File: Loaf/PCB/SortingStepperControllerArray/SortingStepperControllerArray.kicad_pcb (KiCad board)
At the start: 2 copper layers, 100 x 73 mm, 26 parts, among them J1 Conn_01x04_Socket, J2 Conn_01x04_Socket, J3 Conn_01x04_Socket, J4 Conn_01x04_Socket, J5 Motor_Supply, J6 Logic_Supply, J7 Logic_Input, SW1 Limit_Switch, SW2 Limit_Switch, SW3 Limit_Switch, SW4 Limit_Switch

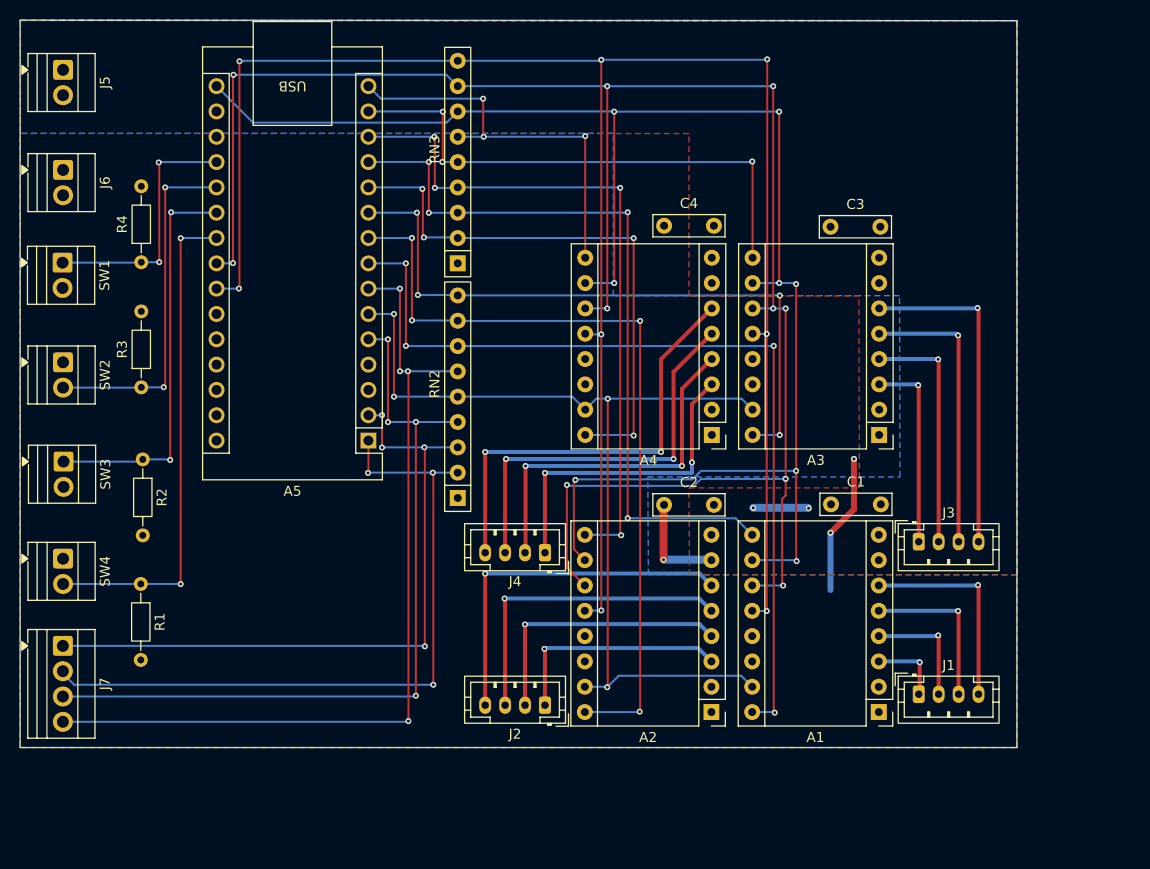
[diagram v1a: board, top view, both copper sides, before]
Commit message: Reoriented board for less signal interference
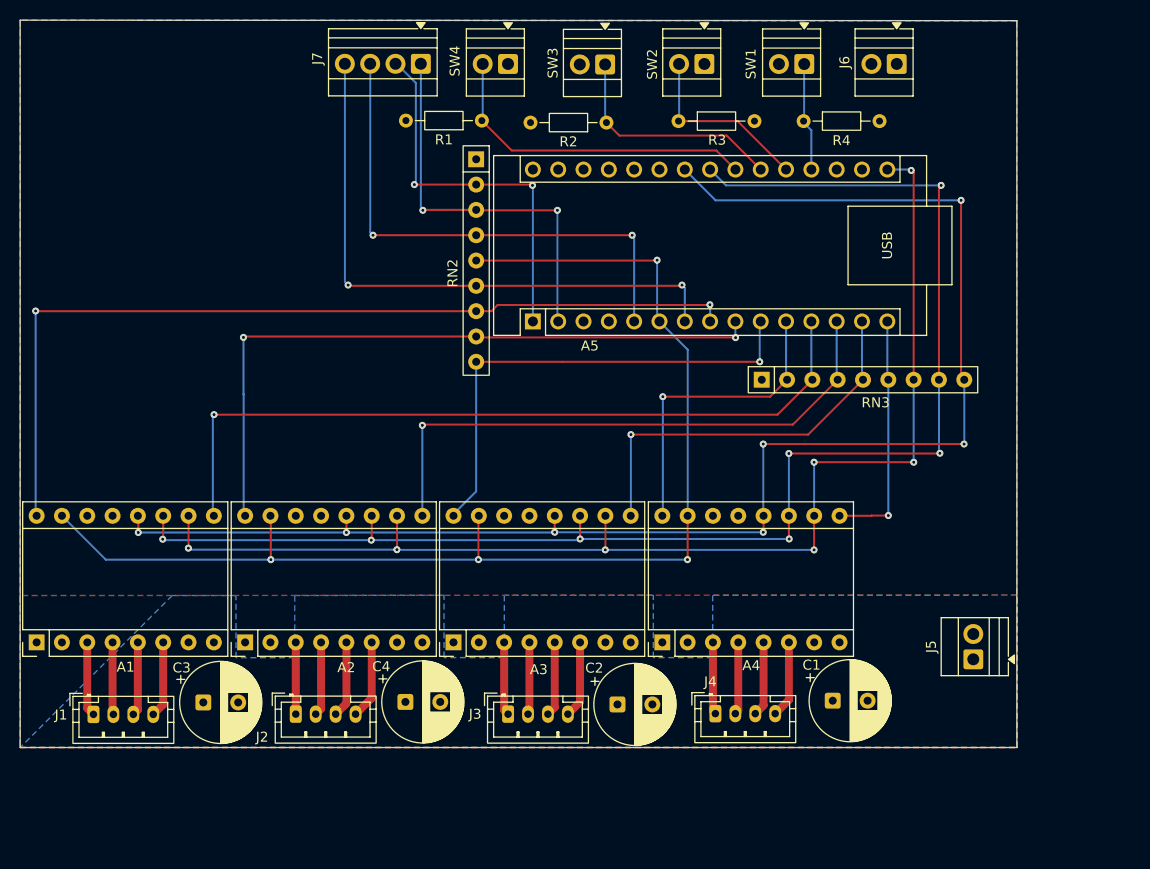
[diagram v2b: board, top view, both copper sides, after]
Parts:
- C1, C2, C3, C4: footprint Capacitor_THT:C_Rect_L7.0mm_W2.0mm_P5.00mm -> Capacitor_THT:CP_Radial_D8.0mm_P3.50mm
- moved J5 108.8 mm to (193.2, 120.5), turned to 90 degrees
- moved A1 84.8 mm to (99.2, 118.8), turned to 90 degrees
- moved J6 84.3 mm to (185.5, 60.8), turned to 180 degrees
- moved J1 82.8 mm to (105.0, 126.1)
- moved C3 79.0 mm to (116.0, 124.9)
- moved SW1 77.0 mm to (176.3, 60.8), turned to 180 degrees
- moved SW2 71.0 mm to (166.2, 60.8), turned to 180 degrees
- moved J7 68.6 mm to (137.8, 60.8), turned to 180 degrees
- moved R4 67.9 mm to (176.2, 66.5), turned to 0 degrees
- moved SW3 67.4 mm to (156.3, 60.9), turned to 180 degrees
- moved SW4 66.8 mm to (146.5, 60.8), turned to 180 degrees
- moved R3 60.2 mm to (163.7, 66.5), turned to 0 degrees
- moved R1 57.7 mm to (143.9, 66.5), turned to 180 degrees
- moved R2 57.5 mm to (156.4, 66.7), turned to 180 degrees
- moved C4 54.4 mm to (136.2, 124.8)
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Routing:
- net /MODE_1: track 189.6 -> 144.7 mm, vias 10 -> 7
- net /MODE_2: track 194.9 -> 150.4 mm, vias 8 -> 7
- net /MODE_0: track 163.9 -> 123.6 mm, vias 8 -> 7
- net Net-(A4-B2): track 44.3 -> 7.72 mm, vias 2 -> 0
- net Net-(A4-B1): track 40.4 -> 7.50 mm, vias 2 -> 0
- net /Motor_2: track 71.5 -> 38.7 mm, vias 3 -> 2
- net /Motor_1: track 68.8 -> 39.6 mm, vias 4 -> 2
- net Net-(A4-A1): track 36.4 -> 7.27 mm, vias 2 -> 0
- net Net-(A2-B2): track 36.4 -> 7.87 mm, vias 1 -> 0
- net /Motor_3: track 80.4 -> 52.2 mm, vias 4 -> 2
- net /STEP: track 95.0 -> 122.9 mm
- net /Motor_4: track 87.3 -> 59.8 mm, vias 4 -> 2
- net Net-(A3-B2): track 33.4 -> 7.71 mm, vias 1 -> 0
- net Net-(A4-A2): track 32.4 -> 7.25 mm, vias 2 -> 0
- net /Motor_4_DIR: track 56.2 -> 31.0 mm, vias 4 -> 1
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
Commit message: Redid the stepper board
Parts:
- removed A5: Arduino_Nano_Every, Module:Arduino_Nano
- removed RN2, RN3: 10K Resistor Array, Resistor_THT:R_Array_SIP9
- added A6: RaspberryPi_Pico, Module:RaspberryPi_Pico_Common_Unspecified, F.Cu at (180.3, 94.1)
- added H1: MountingHole_Pad, MountingHole:MountingHole_3.2mm_M3_DIN965_Pad, F.Cu at (113.0, 68.5)
- added H2: MountingHole_Pad, MountingHole:MountingHole_3.2mm_M3_DIN965_Pad, F.Cu at (205.0, 68.5)
- added H3: MountingHole_Pad, MountingHole:MountingHole_3.2mm_M3_DIN965_Pad, F.Cu at (113.0, 109.5)
- added H4: MountingHole_Pad, MountingHole:MountingHole_3.2mm_M3_DIN965_Pad, F.Cu at (205.0, 109.5)
- added Logo1: Logo_Open_Hardware_Small, Symbol:OSHW-Symbol_6.7x6mm_SilkScreen, F.Cu at (120.3, 68.6)
- added R5: 10K, Resistor_SMD:R_1206_3216Metric_Pad1.30x1.75mm_HandSolder, B.Cu at (176.5, 120.9)
- added R6: 10K, Resistor_SMD:R_1206_3216Metric_Pad1.30x1.75mm_HandSolder, B.Cu at (158.8, 120.9)
- added R7: 10K, Resistor_SMD:R_1206_3216Metric_Pad1.30x1.75mm_HandSolder, B.Cu at (197.8, 111.5)
- added R8: 10K, Resistor_SMD:R_1206_3216Metric_Pad1.30x1.75mm_HandSolder, B.Cu at (181.6, 120.9)
- added RN1: 10K Resistor Array, Resistor_THT:R_Array_SIP9, F.Cu at (201.9, 80.9)
- J1, J2, J3, J4: footprint Connector_JST:JST_PH_B4B-PH-K_1x04_P2.00mm_Vertical -> Connector_JST:JST_XH_B4B-XH-A_1x04_P2.50mm_Vertical
- R1, R2, R3, R4: footprint Resistor_THT:R_Axial_DIN0204_L3.6mm_D1.6mm_P7.62mm_Horizontal -> Resistor_SMD:R_1206_3216Metric_Pad1.30x1.75mm_HandSolder; moved to B.Cu
- moved R2 68.7 mm to (113.0, 119.9), turned to 90 degrees
- moved R4 67.7 mm to (135.9, 120.9), turned to 90 degrees
- moved C4 66.6 mm to (201.9, 136.0), turned to 90 degrees
- moved C3 64.1 mm to (179.1, 136.0), turned to 90 degrees
- moved R1 56.0 mm to (130.8, 120.9), turned to 90 degrees
- moved R3 55.2 mm to (153.7, 120.8), turned to 90 degrees
- moved C1 47.1 mm to (133.3, 136.0), turned to 90 degrees
- moved J4 28.2 mm to (194.3, 134.4), turned to 180 degrees
- moved J3 26.2 mm to (171.4, 134.4), turned to 180 degrees
- moved J2 24.7 mm to (148.6, 134.4), turned to 180 degrees
- moved J7 24.3 mm to (160.8, 68.7)
- moved SW4 24.0 mm to (169.2, 68.7)
- moved J1 22.3 mm to (125.7, 134.4), turned to 180 degrees
- moved A4 21.6 mm to (181.6, 128.0)
- moved SW3 21.2 mm to (176.0, 68.7)
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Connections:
- A1 pad 1: GND2 -> GND
- A1 pad 15: /STEP -> /Step1
- A1 pad 2: GND2 -> GND
- A1 pad 7: GND1 -> GND
- A2 pad 1: GND2 -> GND
- A2 pad 15: /STEP -> /Step2
- A2 pad 2: GND2 -> GND
- A2 pad 7: GND1 -> GND
- A3 pad 1: GND2 -> GND
- A3 pad 15: /STEP -> /Step3
- A3 pad 2: GND2 -> GND
- A3 pad 7: GND1 -> GND
- A4 pad 1: GND2 -> GND
- A4 pad 15: /STEP -> /Step4
- A4 pad 2: GND2 -> GND
- A4 pad 7: GND1 -> GND
- C1 pad 1: GND1 -> GND
- C2 pad 1: GND1 -> GND
- C3 pad 1: GND1 -> GND
- C4 pad 1: GND1 -> GND
- J1 pad 1: Net-(A1-A2) -> Net-(A1-B2)
- J1 pad 2: Net-(A1-A1) -> Net-(A1-B1)
- J1 pad 3: Net-(A1-B1) -> Net-(A1-A1)
- J1 pad 4: Net-(A1-B2) -> Net-(A1-A2)
- J2 pad 1: Net-(A2-A2) -> Net-(A2-B2)
- J2 pad 2: Net-(A2-A1) -> Net-(A2-B1)
- J2 pad 3: Net-(A2-B1) -> Net-(A2-A1)
- J2 pad 4: Net-(A2-B2) -> Net-(A2-A2)
- J3 pad 1: Net-(A3-A2) -> Net-(A3-B2)
- J3 pad 2: Net-(A3-A1) -> Net-(A3-B1)
- J3 pad 3: Net-(A3-B1) -> Net-(A3-A1)
- J3 pad 4: Net-(A3-B2) -> Net-(A3-A2)
- J4 pad 1: Net-(A4-A2) -> Net-(A4-B2)
- J4 pad 2: Net-(A4-A1) -> Net-(A4-B1)
- J4 pad 3: Net-(A4-B1) -> Net-(A4-A1)
- J4 pad 4: Net-(A4-B2) -> Net-(A4-A2)
- J5 pad 1: GND1 -> VMOT
- J5 pad 2: VMOT -> GND
- J6 pad 1: GND2 -> GND
- R1 pad 1: /Limit_4 -> GND
- R1 pad 2: GND2 -> /Motor_1_EN
- R2 pad 1: /Limit_3 -> GND
- R2 pad 2: GND2 -> /Motor_1_DIR
- R3 pad 1: /Limit_2 -> GND
- R3 pad 2: GND2 -> /Motor_2_EN
- R4 pad 1: /Limit_1 -> GND
- R4 pad 2: GND2 -> /Motor_2_DIR
- SW2 pad 1: +5V -> /Limit_2
- SW2 pad 2: /Limit_2 -> +5V
- SW4 pad 1: +5V -> /Limit_4
- SW4 pad 2: /Limit_4 -> +5V
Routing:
- net +5V: track 0.00 -> 218.5 mm, vias 0 -> 9
- net /STEP: track 122.9 -> 0.00 mm, vias 4 -> 0
- net /Step1: track 0.00 -> 101.3 mm, vias 0 -> 2
- net /Step2: track 0.00 -> 65.4 mm, vias 0 -> 2
- net /MODE_2: track 150.4 -> 90.4 mm, vias 7 -> 5
- net /MODE_1: track 144.7 -> 88.5 mm, vias 7 -> 5
- net /MODE_0: track 123.6 -> 86.6 mm, vias 7 -> 5
- net /Motor_3_DIR: track 49.0 -> 17.4 mm, vias 1 -> 0
- net /Step4: track 0.00 -> 26.7 mm, vias 0 -> 2
- net VMOT: track 0.00 -> 22.0 mm
- net /Motor_1_DIR: track 90.2 -> 109.5 mm
- net /Limit_1: track 11.1 -> 28.7 mm, vias 0 -> 2
- net /Motor_4_EN: track 24.7 -> 40.3 mm, vias 1 -> 2
- net /Motor_4: track 59.8 -> 45.0 mm
- net /Limit_2: track 18.7 -> 33.0 mm, vias 0 -> 2
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- added copper zone on B.Cu, net GND
- added copper zone on F.Cu, net GND
- removed copper zone on F.Cu, net +5V
- removed copper zone on B.Cu, net GND1
- removed copper zone on B.Cu, net GND2
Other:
- board size 100 x 73 mm -> 100 x 75 mm
- board text added: "4 Stepper control Board oshe.io REV 2026"

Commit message: Updated control board footprints
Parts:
- J5, J6, SW1, SW2, SW3, SW4: footprint TerminalBlock:TerminalBlock_Xinya_XY308-2.54-2P_1x02_P2.54mm_Horizontal -> TerminalBlock_TE-Connectivity:TerminalBlock_TE_282834-2_1x02_P2.54mm_Horizontal
- J7: footprint TerminalBlock:TerminalBlock_Xinya_XY308-2.54-4P_1x04_P2.54mm_Horizontal -> TerminalBlock_TE-Connectivity:TerminalBlock_TE_282834-4_1x04_P2.54mm_Horizontal
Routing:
- net +5V: track 218.5 -> 221.4 mm

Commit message: Peter recommended PCB changes
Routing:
- net +5V: track 221.4 -> 217.7 mm
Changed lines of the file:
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@@
 	)
 	(segment
-		(start 178.158 66.525)
-		(end 178.64 67.007)
-		(width 1)
-		(layer "F.Cu")
-		(net "+5V")
-	)
-	(segment
-		(start 143.458 115.253)
-		(end 145.658 117.453)
+		(start 180.34 66.525)
+		(end 180.34 68.707)
+		(width 1)
+		(layer "F.Cu")
+		(net "+5V")
+	)
+	(segment
+		(start 122.787 117.453)
+		(end 197.978 117.453)
+		(width 1)
+		(layer "F.Cu")
+		(net "+5V")
+	)
+	(segment
+		(start 195.585 68.585)
+		(end 195.585 68.707)
 		(width 1)
 		(layer "F.Cu")
@@
 	)
 	(segment
+		(start 193.525 66.525)
+		(end 195.585 68.585)
+		(width 1)
+		(layer "F.Cu")
+		(net "+5V")
+	)
+	(segment
+		(start 173.482 66.525)
+		(end 173.482 68.707)
+		(width 1)
+		(layer "F.Cu")
+		(net "+5V")
+	)
+	(segment
 		(start 163.83 115.316)
 		(end 166.37 115.316)
@@
 	)
 	(segment
-		(start 168.518 117.453)
-		(end 191.378 117.453)
-		(width 1)
-		(layer "F.Cu")
-		(net "+5V")
-	)
-	(segment
 		(start 197.978 117.453)
 		(end 198.978 117.453)
@@
 	)
 	(segment
-		(start 173.482 68.707)
-		(end 171.782 67.007)
+		(start 166.624 68.707)
+		(end 166.624 68.29657)
+		(width 1)
+		(layer "F.Cu")
+		(net "+5V")
+	)
+	(segment
+		(start 166.37 115.305)
+		(end 166.37 117.453)
 		(width 1)
 		(layer "F.Cu")
@@
 	)
 	(segment
-		(start 191.378 117.453)
-		(end 197.978 117.453)
-		(width 1)
-		(layer "F.Cu")
-		(net "+5V")
-	)
-	(segment
 		(start 185.016 66.525)
-		(end 193.403 66.525)
-		(width 1)
-		(layer "F.Cu")
-		(net "+5V")
-	)
-	(segment
-		(start 187.198 68.707)
-		(end 185.498 67.007)
+		(end 187.198 66.525)
 		(width 1)
 		(layer "F.Cu")
@@
 	)
 	(segment
+		(start 143.51 115.305)
+		(end 143.51 117.453)
+		(width 1)
+		(layer "F.Cu")
+		(net "+5V")
+	)
+	(segment
 		(start 198.978 117.453)
 		(end 199.978 117.453)
@@
 	)
 	(segment
-		(start 145.658 117.453)
-		(end 168.518 117.453)
-		(width 1)
-		(layer "F.Cu")
-		(net "+5V")
-	)
-	(segment
 		(start 189.178 115.253)
-		(end 191.378 117.453)
+		(end 189.23 115.305)
+		(width 1)
+		(layer "F.Cu")
+		(net "+5V")
+	)
+	(segment
+		(start 120.598 115.253)
+		(end 120.598 115.264)
 		(width 1)
 		(layer "F.Cu")
@@
 	)
 	(segment
+		(start 187.198 66.525)
+		(end 193.525 66.525)
+		(width 1)
+		(layer "F.Cu")
+		(net "+5V")
+	)
+	(segment
 		(start 195.58 73.02)
 		(end 196.337 72.263)
@@
 	)
 	(segment
-		(start 166.624 67.292787)
-		(end 167.391787 66.525)
-		(width 1)
-		(layer "F.Cu")
-		(net "+5V")
-	)
-	(segment
-		(start 166.624 68.707)
-		(end 166.624 67.292787)
-		(width 1)
-		(layer "F.Cu")
-		(net "+5V")
-	)
-	(segment
-		(start 122.798 117.453)
-		(end 145.658 117.453)
-		(width 1)
-		(layer "F.Cu")
-		(net "+5V")
-	)
-	(segment
-		(start 185.016 66.525)
-		(end 185.498 67.007)
+		(start 189.23 115.305)
+		(end 189.23 117.453)
+		(width 1)
+		(layer "F.Cu")
+		(net "+5V")
+	)
+	(segment
+		(start 187.198 66.525)
+		(end 187.198 68.707)
+		(width 1)
+		(layer "F.Cu")
+		(net "+5V")
+	)
+	(segment
+		(start 166.624 68.29657)
+		(end 168.39557 66.525)
+		(width 1)
+		(layer "F.Cu")
+		(net "+5V")
+	)
+	(segment
+		(start 168.39557 66.525)
+		(end 173.482 66.525)
 		(width 1)
 		(layer "F.Cu")
@@
 	)
 	(segment
-		(start 171.3 66.525)
-		(end 171.782 67.007)
+		(start 166.318 115.253)
+		(end 166.37 115.305)
 		(width 1)
 		(layer "F.Cu")
@@
 	(segment
 		(start 178.158 66.525)
-		(end 185.016 66.525)
-		(width 1)
-		(layer "F.Cu")
-		(net "+5V")
-	)
-	(segment
-		(start 166.318 115.253)
-		(end 168.518 117.453)
+		(end 180.34 66.525)
 		(width 1)
 		(layer "F.Cu")
@@
 	)
 	(segment
-		(start 120.598 115.253)
-		(end 122.798 117.453)
+		(start 180.34 66.525)
+		(end 185.016 66.525)
+		(width 1)
+		(layer "F.Cu")
+		(net "+5V")
+	)
+	(segment
+		(start 120.598 115.264)
+		(end 122.787 117.453)
 		(width 1)
 		(layer "F.Cu")
@@
 	)
 	(segment
+		(start 143.458 115.253)
+		(end 143.51 115.305)
+		(width 1)
+		(layer "F.Cu")
+		(net "+5V")
+	)
+	(segment
 		(start 196.337 72.263)
 		(end 196.337 72.258)
 		(width 1)
 		(layer "F.Cu")
-		(net "+5V")
-	)
-	(segment
-		(start 167.391787 66.525)
-		(end 171.3 66.525)
-		(width 1)
-		(layer "F.Cu")
-		(net "+5V")
-	)
-	(segment
-		(start 193.403 66.525)
-		(end 195.585 68.707)
-		(width 1)
-		(layer "F.Cu")
-		(net "+5V")
-	)
-	(segment
-		(start 180.34 68.707)
-		(end 178.64 67.007)
-		(width 1)
-		(layer "F.Cu")
